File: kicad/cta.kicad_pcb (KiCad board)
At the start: 2 copper layers, 50.8 x 50.8 mm, 24 parts, among them Q1 2N3904, Q2 2N3906, U1 LM324

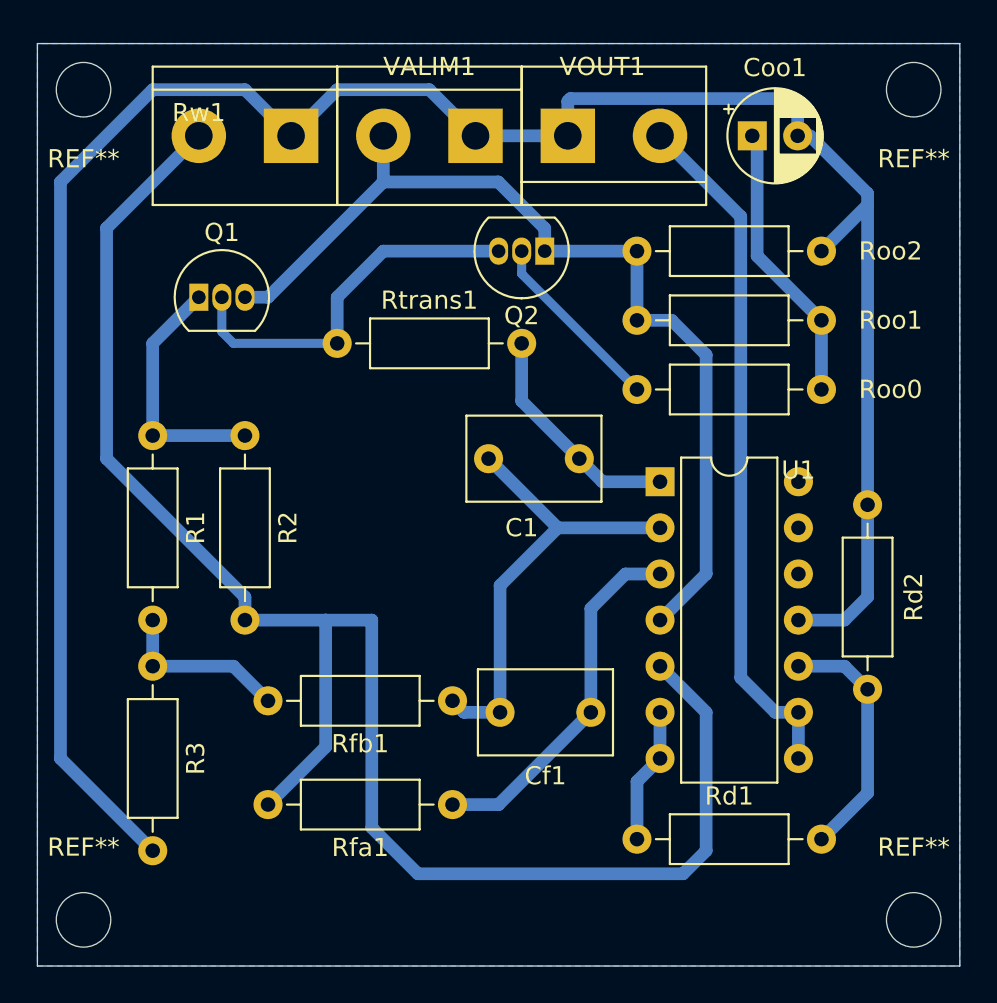
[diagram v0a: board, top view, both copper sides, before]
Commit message: Improved board layout and allowed for a power resistor.
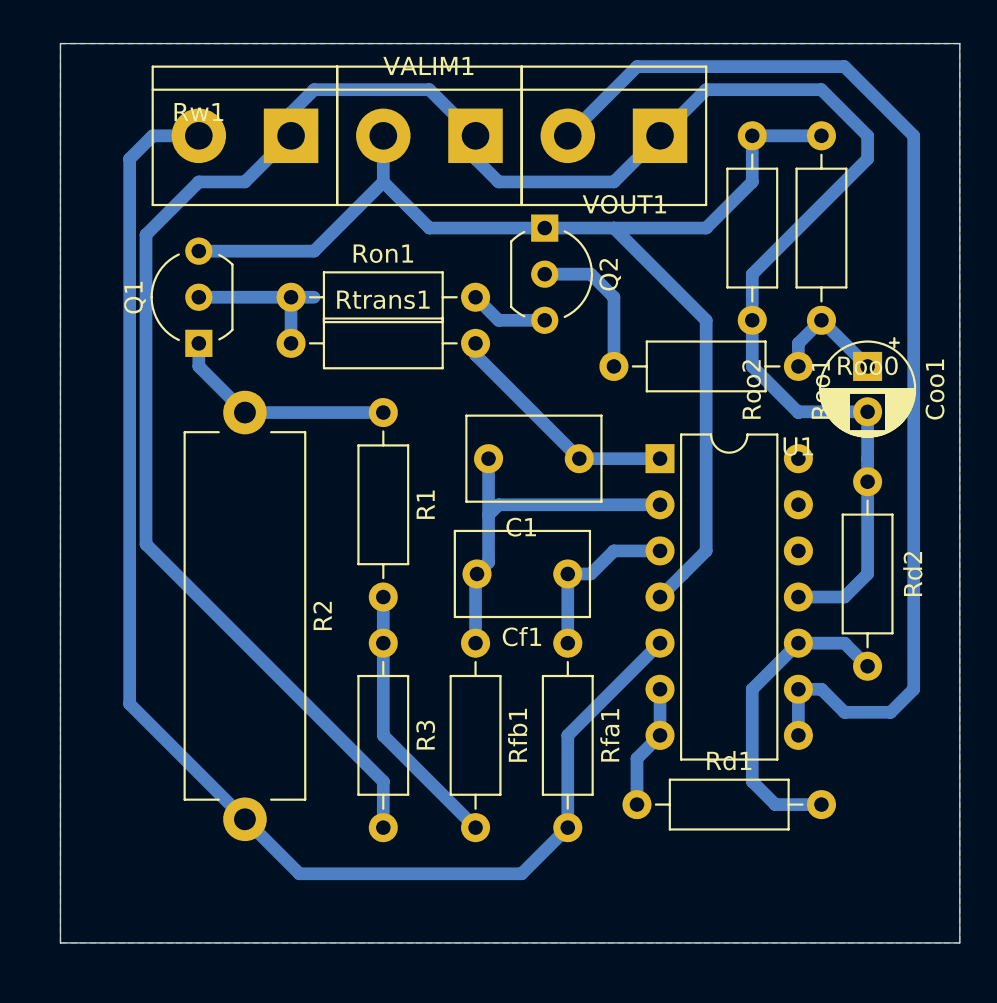
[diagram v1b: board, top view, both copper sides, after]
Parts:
- removed REF** (x4): MountingHole_3mm, MountingHole:MountingHole_3mm
- added Ron1: 2k, Resistor_THT:R_Axial_DIN0207_L6.3mm_D2.5mm_P10.16mm_Horizontal, F.Cu at (102.9, 77.5)
- Q1, Q2: footprint Package_TO_SOT_THT:TO-92_Inline -> Package_TO_SOT_THT:TO-92_Inline_Wide
- R2: footprint Resistor_THT:R_Axial_DIN0207_L6.3mm_D2.5mm_P10.16mm_Horizontal -> Resistor_THT:R_Axial_Power_L20.0mm_W6.4mm_P22.40mm
- Rtrans1: value 1k -> 2k
- moved Roo1 14.4 mm to (132.1, 68.6), turned to 270 degrees
- moved Coo1 14.2 mm to (134.6, 81.3), turned to 270 degrees
- moved R1 12.8 mm to (108.0, 83.8)
- moved R3 12.8 mm to (108.0, 96.5)
- moved Rfa1 10.9 mm to (118.1, 96.5), turned to 270 degrees
- moved Roo2 8.98 mm to (128.3, 68.6), turned to 270 degrees
- moved Cf1 7.73 mm to (118.1, 92.7)
- moved VOUT1 5.08 mm to (123.2, 68.6), turned to 180 degrees
- moved Rfb1 3.42 mm to (113.0, 96.5), turned to 270 degrees
- moved Q1 2.54 mm to (97.8, 80.0), turned to 90 degrees
- moved Rtrans1 2.54 mm to (102.9, 80.0)
- moved Rd1 1.91 mm to (121.9, 105.4)
- moved Roo0 1.80 mm to (130.8, 81.3)
- moved Q2 1.27 mm to (116.8, 73.7), turned to 270 degrees
- moved R2 1.27 mm to (100.3, 83.8)
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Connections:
- Q2 pad 3: Net-(Q1-Pad2) -> Net-(Q2-Pad3)
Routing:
- net Net-(U1-Pad8): track 38.2 -> 62.6 mm
- net Net-(R2-Pad2): track 93.0 -> 75.7 mm
- net +24V: track 53.1 -> 66.5 mm
- net Net-(Q1-Pad2): track 21.0 -> 8.89 mm
- net Net-(Cf1-Pad1): track 20.0 -> 9.42 mm
- net Net-(Coo1-Pad1): track 15.5 -> 6.66 mm
- net Net-(C1-Pad2): track 25.4 -> 20.1 mm
- net Net-(R1-Pad2): track 9.68 -> 14.8 mm
- net Net-(Q2-Pad3): track 0.00 -> 4.34 mm
- net Net-(Rd1-Pad2): track 13.6 -> 17.3 mm
- net Net-(Q2-Pad2): track 10.3 -> 8.15 mm
- net Net-(Q1-Pad1): track 13.8 -> 12.5 mm
- net Net-(Rd1-Pad1): track 7.51 -> 6.88 mm
- net Net-(C1-Pad1): track 12.6 -> 13.2 mm
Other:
- board size 50.8 x 50.8 mm -> 49.5 x 49.5 mm

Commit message: Removed a terminal block and increased the power termninal block to 3
The circuit uses the same ground for power and signal. So I removed the signal terminal block and added another terminal to the power terminal block
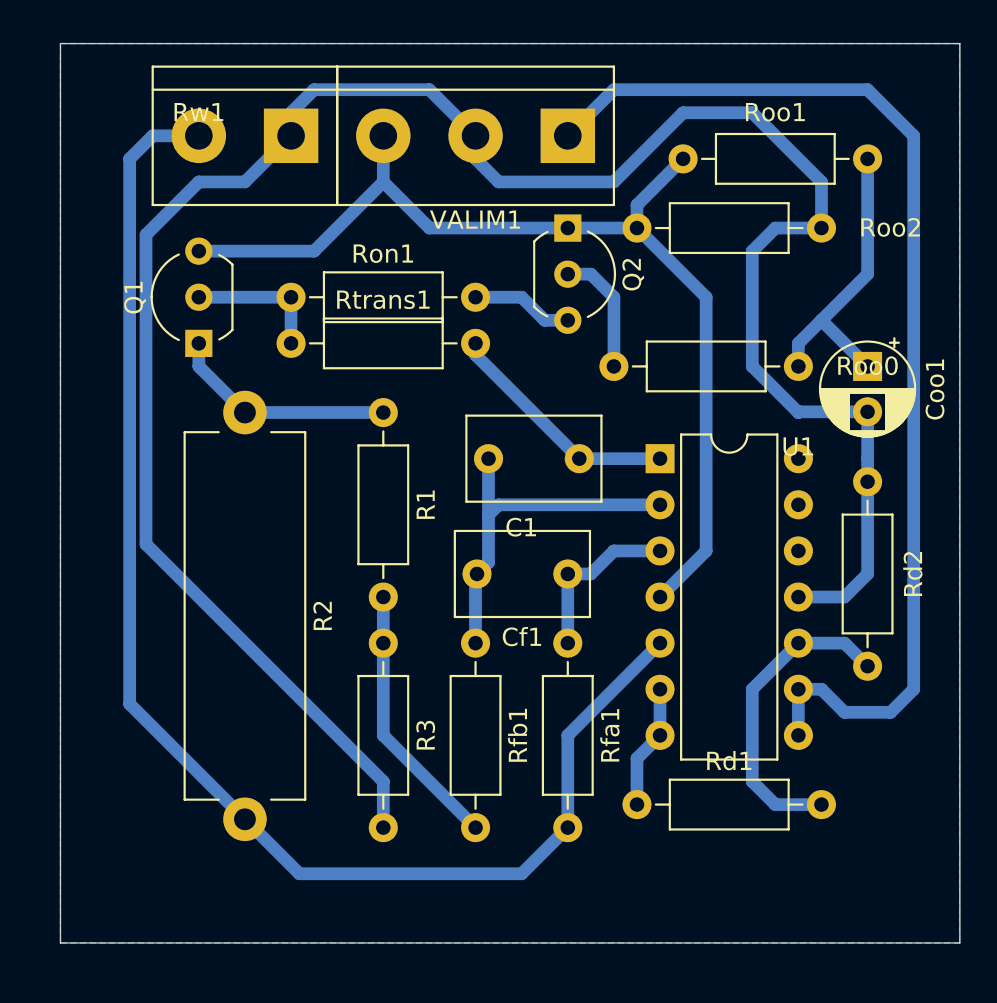
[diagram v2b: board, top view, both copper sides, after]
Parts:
- removed VOUT1: VOUT, TerminalBlock:TerminalBlock_bornier-2_P5.08mm
- VALIM1: footprint TerminalBlock:TerminalBlock_bornier-2_P5.08mm -> TerminalBlock:TerminalBlock_bornier-3_P5.08mm
- moved Roo2 8.13 mm to (121.9, 73.7), turned to 0 degrees
- moved Roo1 7.73 mm to (124.5, 69.8), turned to 0 degrees
- moved VALIM1 5.08 mm to (118.1, 68.6)
- moved Q2 1.27 mm to (118.1, 73.7)
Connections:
- VALIM1 pad 1: GNDPWR -> Net-(U1-Pad8)
- VALIM1 pad 2: +24V -> GNDPWR
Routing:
- net Net-(Coo1-Pad1): track 6.66 -> 16.6 mm
- net +24V: track 66.5 -> 57.1 mm
- net GNDPWR: track 123.9 -> 119.2 mm
- net Net-(Q2-Pad2): track 8.15 -> 6.88 mm
- net Net-(Q1-Pad2): track 8.89 -> 7.62 mm
- net Net-(Q2-Pad3): track 4.34 -> 5.61 mm
- net Net-(U1-Pad8): track 62.6 -> 61.6 mm

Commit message: Forgot to add mounting holes
Now I have to test this new board
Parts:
- added REF**: MountingHole_3mm, MountingHole:MountingHole_3mm, F.Cu at (137.2, 66.0)
- added REF**: MountingHole_3mm, MountingHole:MountingHole_3mm, F.Cu at (137.2, 110.5)
- added REF**: MountingHole_3mm, MountingHole:MountingHole_3mm, F.Cu at (92.7, 110.5)
- added REF**: MountingHole_3mm, MountingHole:MountingHole_3mm, F.Cu at (92.7, 66.0)
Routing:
- net Net-(U1-Pad8): track 61.6 -> 60.8 mm

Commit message: Set new values for components
One of the things I noticed with the circuit is an asymmetry when increasing wind speed vs decreasing. When increasing, the response is fast. But when decreasing it is very low.

This is to be expected: the electronics respond much faster than the cooling: the maximum colling rate happens when there is no current and therefore heat transfer within the thermistor is the slow part.

To make response more symmetric, I increased the the resistors at the op amp input from 1k to 47k. This introduced a new problem: the capacitor would not charge fast enough for the initial charge subcircuit. I could increase the capacitoor in this subcircuit and increase the resistance as well. I haven't tested these solutions. What I did was increase the feedback capacitance from 100nF to 1uF. The circuit is working and the response is much more symmetric.

Another change was decreasing the base resistors. They are not necessary. I still left a low resistor just to keep the layout. But they could be replaced by wires (that's what I tested). This improves response time (which doesn't really matter).
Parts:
- C1: value C -> 1u
- R1: value 150 -> 100
- R2: value 15 -> 10
- R3: value 1.5k -> 1k
- Rfa1, Rfb1: value 1k -> 47k
- Ron1, Rtrans1: value 2k -> 10
- Roo0: value R_US -> 10

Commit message: Replaced transistor KSP2222A for BC517
The BC517 is a darlington transistor and the response of the anemometer is much faster (when increasing wind speed). Why would I care about that if I went to all the trouble to make the response more symmetric?

It really depends on the objective. If I want to measure the mean speed in a turbulent flow, using the more symmetric response is better. But If I want to estimate wind gusts, the faster response time could do that! This change inm transistor really has no downsides.
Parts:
- Q1: value 2N3904 -> BC517
- moved Q1 5.08 mm to (97.8, 74.9), turned to 270 degrees
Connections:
- Q1 pad 1: Net-(Q1-Pad1) -> +24V
- Q1 pad 3: +24V -> Net-(Q1-Pad3)
- R1 pad 1: Net-(Q1-Pad1) -> Net-(Q1-Pad3)
- R2 pad 1: Net-(Q1-Pad1) -> Net-(Q1-Pad3)
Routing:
- net Net-(Q1-Pad3): track 0.00 -> 12.5 mm
- net Net-(Q1-Pad1): track 12.5 -> 0.00 mm

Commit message: I found out the trouble: too much power dissipated on the tranistor
During normal operation, the current is low and therefore the voltage at the top of the bridge is low and the transistor needs to reduce a lot of voltage and dissipate a lot of heat. After normal operation for a little time the transistor would burn up.

I see 2 solutions:
 1. Replace the transistor
 2. Modify the resistors

I think I will do #2 anyway and do #2.
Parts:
- removed REF** (x4): MountingHole_3mm, MountingHole:MountingHole_3mm
- added D1: 1N4148, Diode_THT:D_DO-35_SOD27_P7.62mm_Horizontal, F.Cu at (119.4, 74.9)
- Ron1: value 10 -> 47k
- moved Q2 5.43 mm to (120.0, 78.7), turned to 180 degrees
- moved Rtrans1 0.63 mm to (102.9, 80.6)
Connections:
- Q2 pad 1: +24V -> Net-(D1-Pad1)
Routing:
- net Net-(D1-Pad1): track 0.00 -> 4.07 mm
- net +24V: track 57.1 -> 60.7 mm
- net Net-(Q2-Pad3): track 5.61 -> 2.43 mm
- net Net-(Q2-Pad2): track 6.88 -> 5.34 mm
- net Net-(Q1-Pad2): track 7.62 -> 8.25 mm
- net Net-(C1-Pad1): track 13.2 -> 12.5 mm
- removed copper zone on B.Cu, net GNDPWR

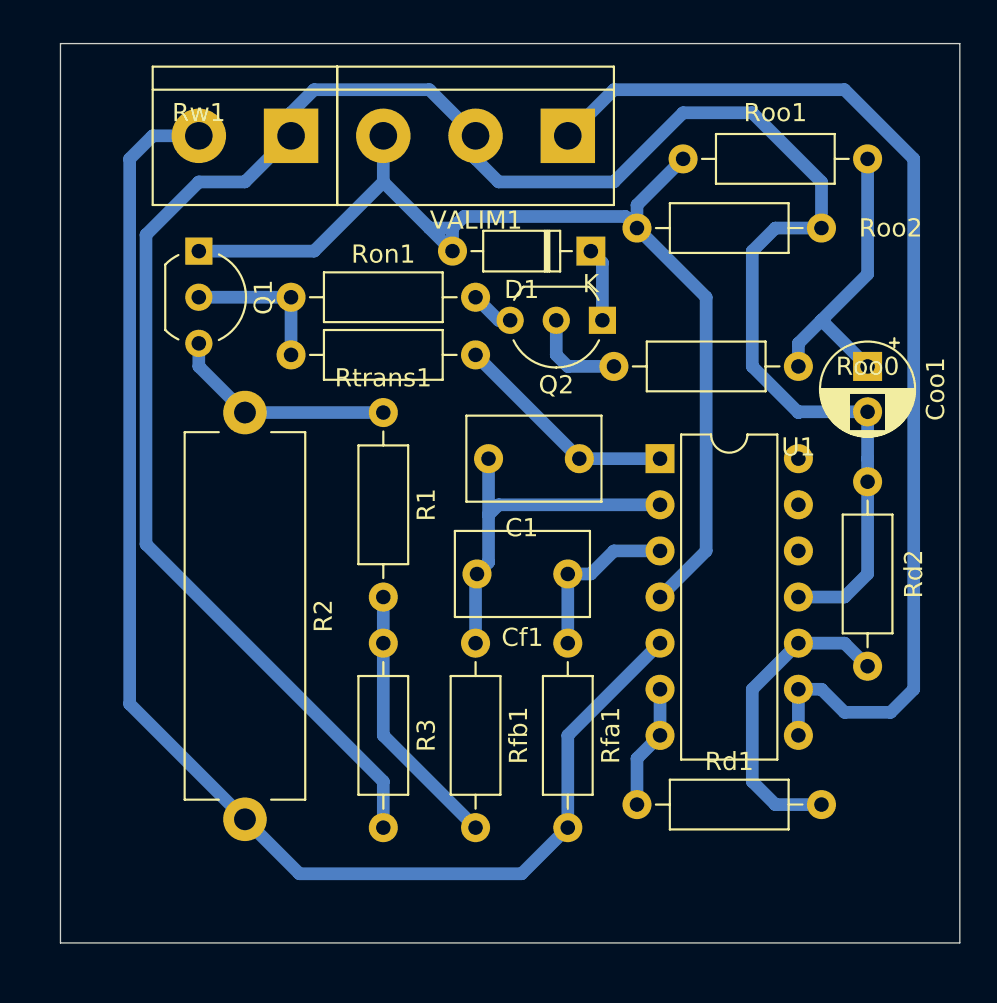
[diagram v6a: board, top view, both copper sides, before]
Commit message: Replaced the transistor from BC517 to TIP120 and resistors on the bridge
The resistors on the top of the bridge now have the same value as on the bottom of the bridge. This decreased the power dissipated in the transistor.

The new transistor can also include a heat sink dependeing on application. The setup is working on the protoboard. I has been working for the last hour, voltage input can be decreased to 15V and the system will still start. At 13V it takes a while, perhaps a larger capacitor for startup procedure will help.
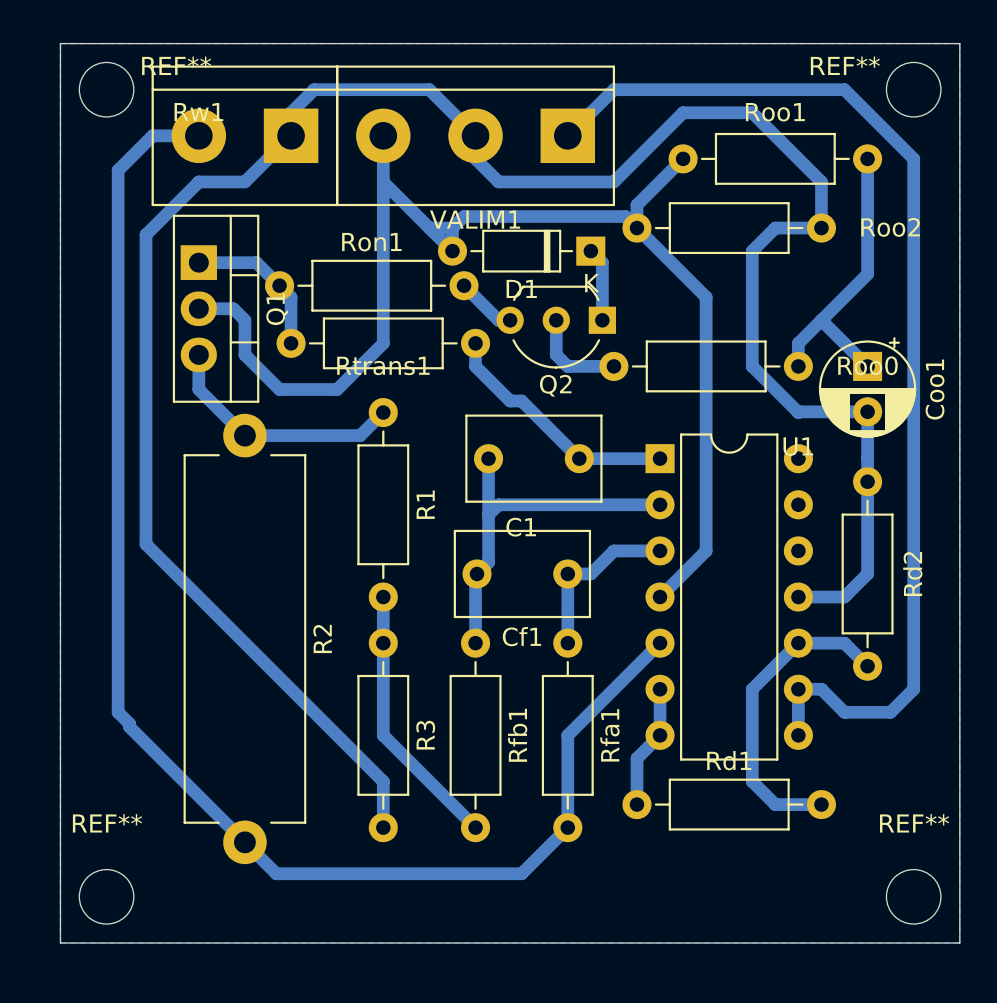
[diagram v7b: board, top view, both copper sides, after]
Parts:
- added REF**: MountingHole_3mm, MountingHole:MountingHole_3mm, F.Cu at (137.2, 110.5)
- added REF**: MountingHole_3mm, MountingHole:MountingHole_3mm, F.Cu at (92.7, 110.5)
- added REF**: MountingHole_3mm, MountingHole:MountingHole_3mm, F.Cu at (92.7, 66.0)
- added REF**: MountingHole_3mm, MountingHole:MountingHole_3mm, F.Cu at (137.2, 66.0)
- Q1: value BC517 -> TIP122; footprint Package_TO_SOT_THT:TO-92_Inline_Wide -> Package_TO_SOT_THT:TO-220-3_Vertical
- moved R2 1.27 mm to (100.3, 85.1)
- moved Ron1 0.90 mm to (102.2, 76.8)
- moved Q1 0.63 mm to (97.8, 75.6)
- moved Rtrans1 0.63 mm to (102.9, 80.0)
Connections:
- Q1 pad 1: +24V -> Net-(Q1-Pad1)
- Q1 pad 2: Net-(Q1-Pad2) -> +24V
- Ron1 pad 1: Net-(Q1-Pad2) -> Net-(Q1-Pad1)
- Rtrans1 pad 1: Net-(Q1-Pad2) -> Net-(Q1-Pad1)
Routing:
- net +24V: track 60.7 -> 72.0 mm
- net Net-(Q1-Pad1): track 0.00 -> 8.41 mm
- net Net-(Q1-Pad2): track 8.25 -> 0.00 mm
- net Net-(R2-Pad2): track 75.7 -> 76.9 mm
- net Net-(Q1-Pad3): track 12.5 -> 13.6 mm
- net Net-(C1-Pad1): track 12.5 -> 13.5 mm
- net Net-(Q2-Pad3): track 2.43 -> 3.33 mm
- added copper zone on B.Cu, net GNDPWR

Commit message: Cleaned up the schematics
The circuit is much clearer! I have tested the circuit 24 hours and it is working. Now I have to test it on a wind tunnel and checkout how well it operates.
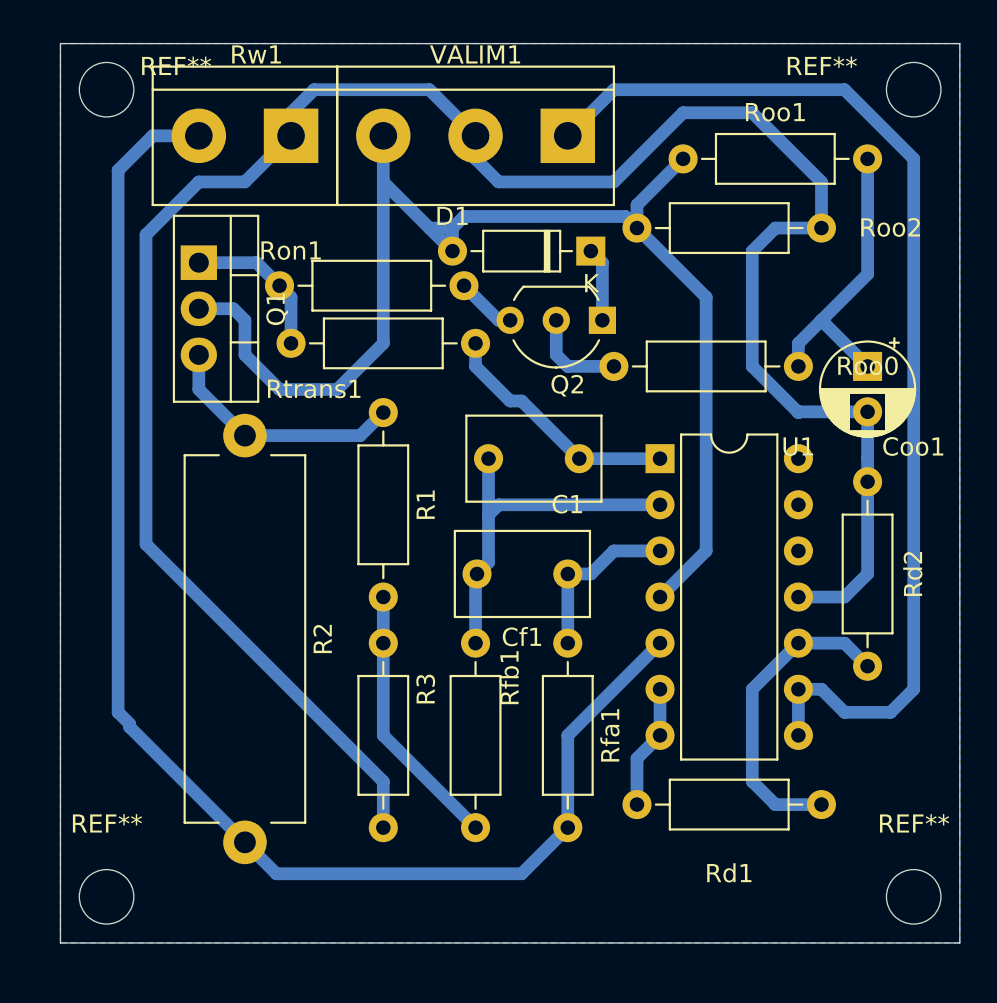
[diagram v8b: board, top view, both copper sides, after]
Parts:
- Q1: value TIP122 -> TIP120
- Q2: value 2N3906 -> KSP2907
- Ron1: value 47k -> 10
- Roo1: value R_US -> 100k
- Roo2: value R_US -> 12k
- Rw1: value Conn_01x02_Male -> Conn
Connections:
- net +24V renamed VCC
- net GNDPWR renamed GND
- net Net-(U1-Pad8) renamed /VOUTPUT
